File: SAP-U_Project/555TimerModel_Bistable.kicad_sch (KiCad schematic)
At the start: 13 parts, among them Q2 BC107, U10 Inverter, U4 Comparator 2, U5 SR LATCH

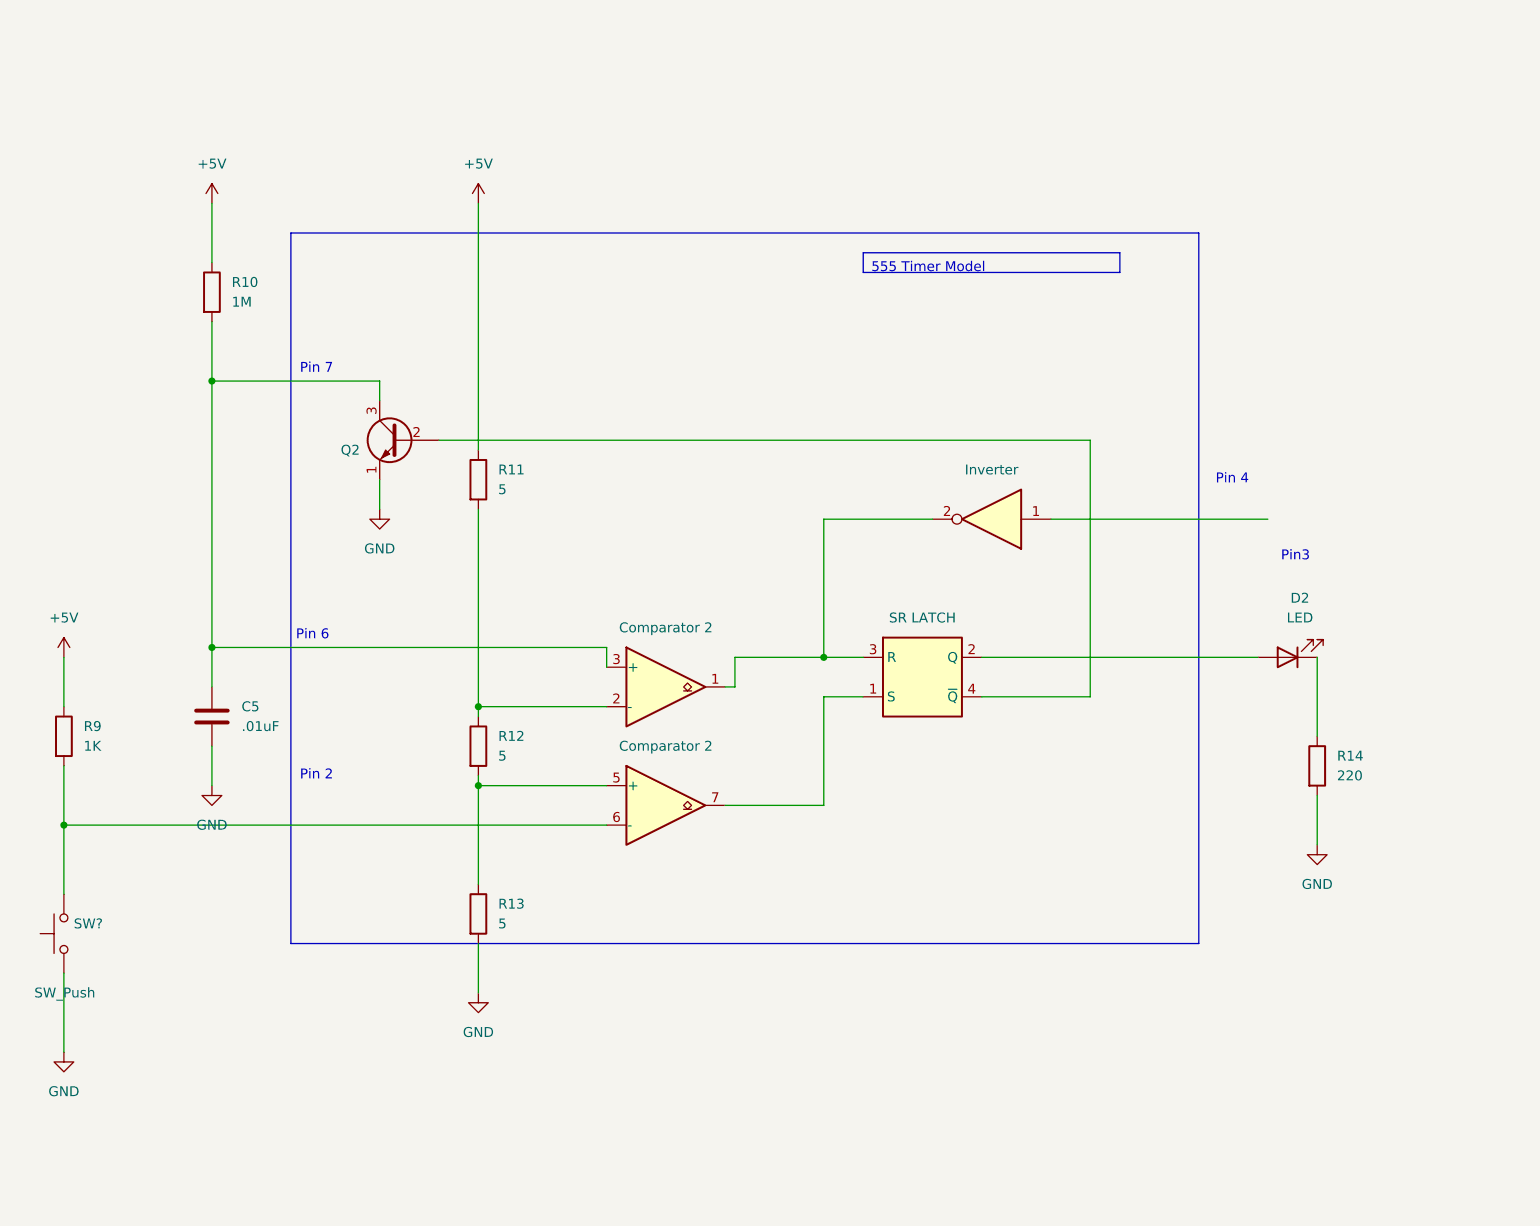
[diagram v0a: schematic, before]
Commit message: Checkpoint: added circuit for Bistable
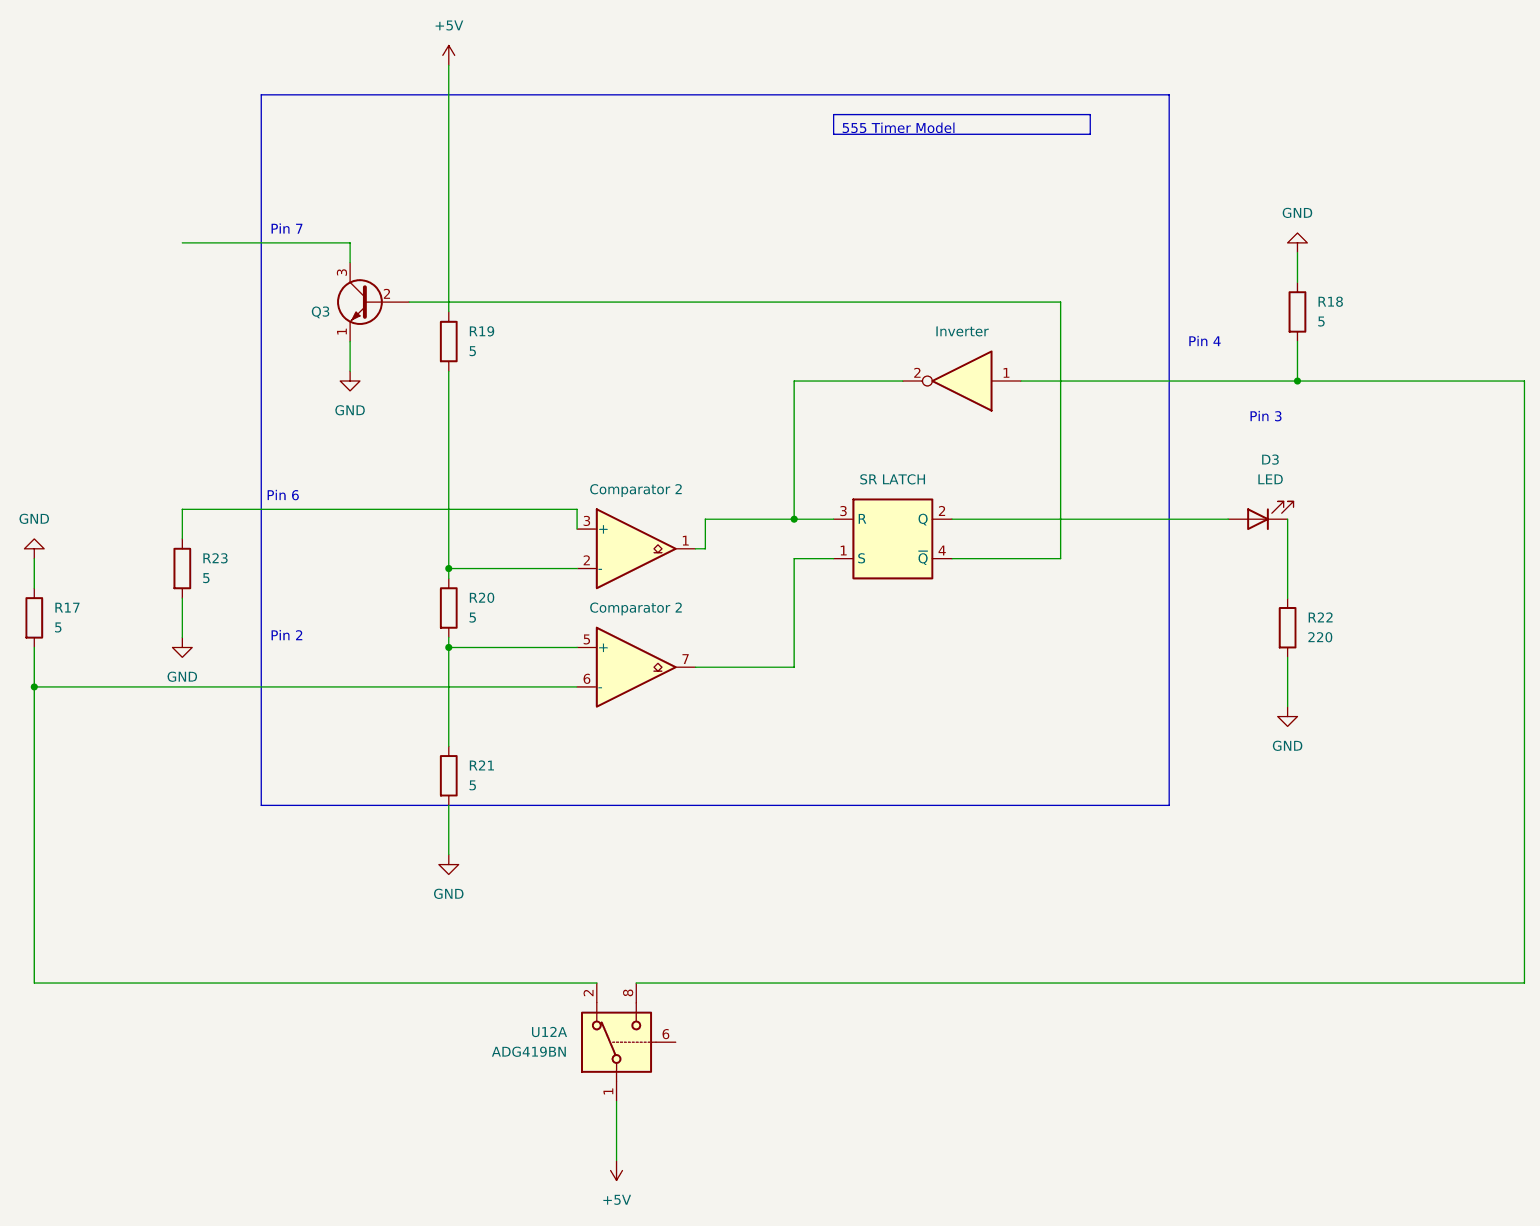
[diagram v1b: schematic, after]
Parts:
- removed C5: .01uF, symbol Device:C
- removed R10: 1M, symbol Device:R
- removed R9: 1K, symbol Device:R
- removed SW?: SW_Push, symbol Switch:SW_Push
- removed U10: Inverter, symbol 74xx:74LS04
- added R17, R18, R23: 5, symbol Device:R
- added U12: ADG419BN, Package_DIP:DIP-8_W7.62mm, symbol Analog_Switch:ADG419BN
- added U9: Inverter, symbol 74xx:74LS04
- renumbered D2 to D3, Q2 to Q3, R11 to R19, R12 to R20, R13 to R21, R14 to R22, U4 to U7, U5 to U8
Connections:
- net +5V: now also U12.1
- net GND: now also R17.1, R18.1, R23.2
- net at U7.6 (-): now also R17.2, U12.2
- net at U7.1, U8.3 (R): now also U9.2
- net at U7.3 (+): now also R23.1; no longer Q3.3 (C)
- new net: R18.2, U12.8, U9.1
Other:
- note added: "Pin 3"
- note removed: "Pin3"
- moved on the sheet: D3, Q3, R19, R20, R21, R22

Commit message: Checkpoint: added switching logic
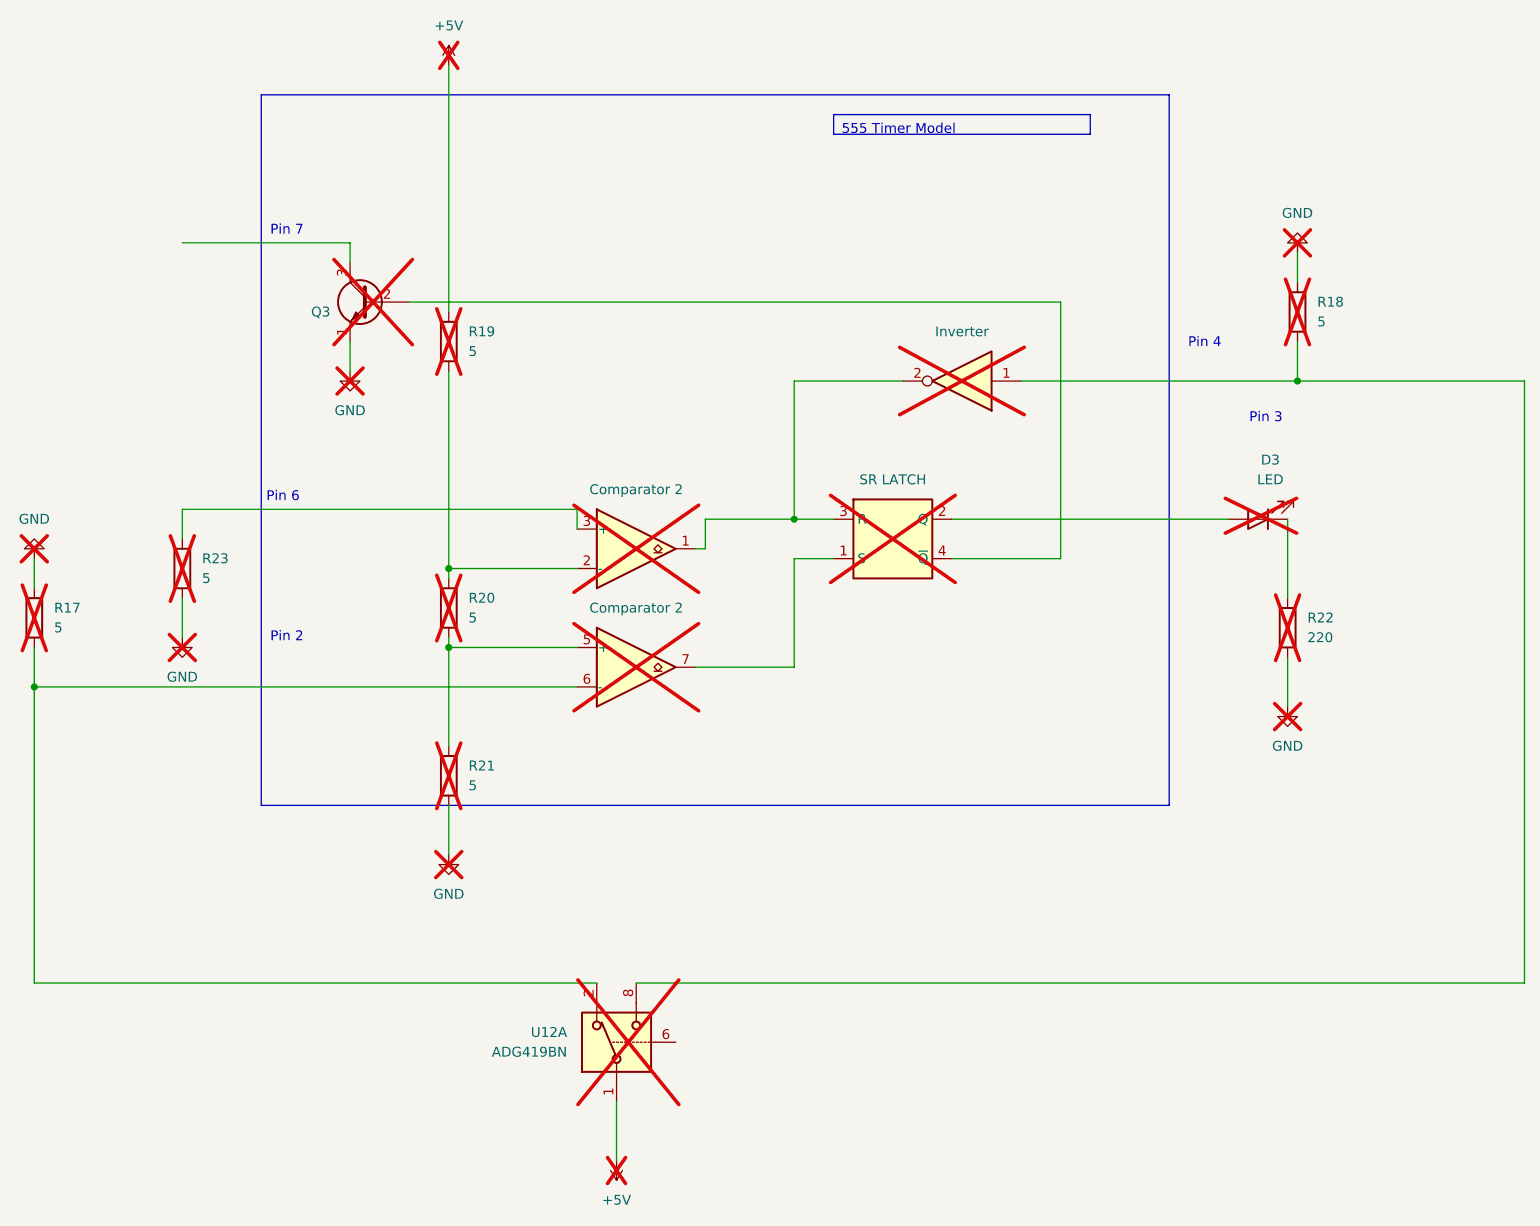
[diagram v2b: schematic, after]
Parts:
- D3, Q3, R17, R18, R19, R20, R21, R22, R23, U12, U7, U8, U9: now not fitted; now left out of the parts list
